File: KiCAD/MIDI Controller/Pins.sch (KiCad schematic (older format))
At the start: 25 parts, among them J10 MJ-3502, J11 MJ-3502, J12 MJ-3502, J13 MJ-3502, J14 MJ-3502, J15 MJ-3502, J16 MJ-3502, J17 MJ-3502, J5 MJ-3502, J6 MJ-3502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

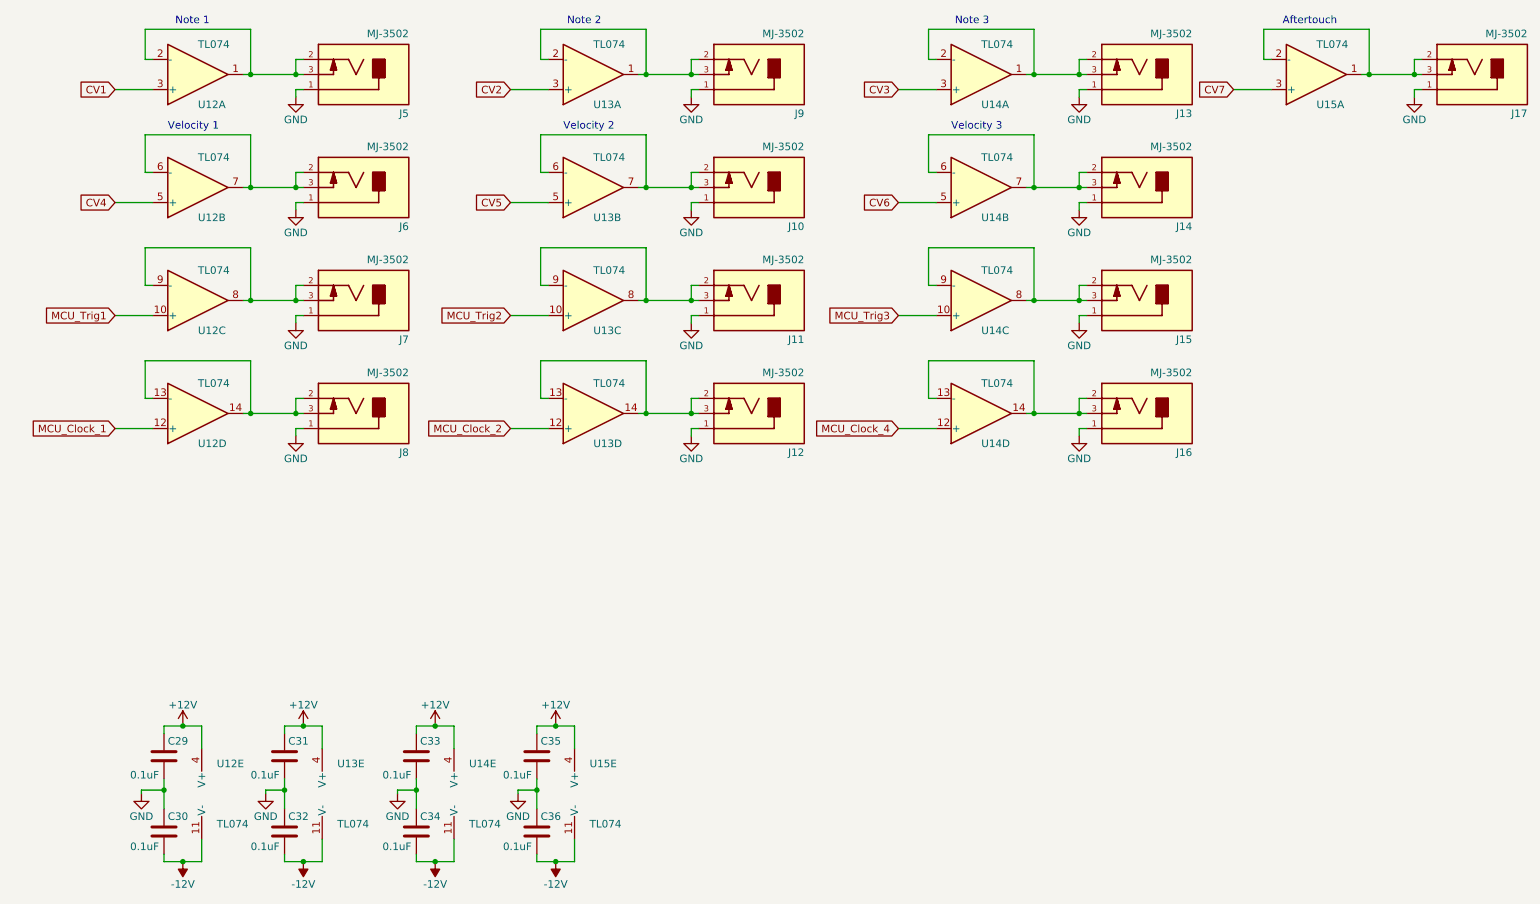
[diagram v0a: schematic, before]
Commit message: Added MIDI controller and PSU
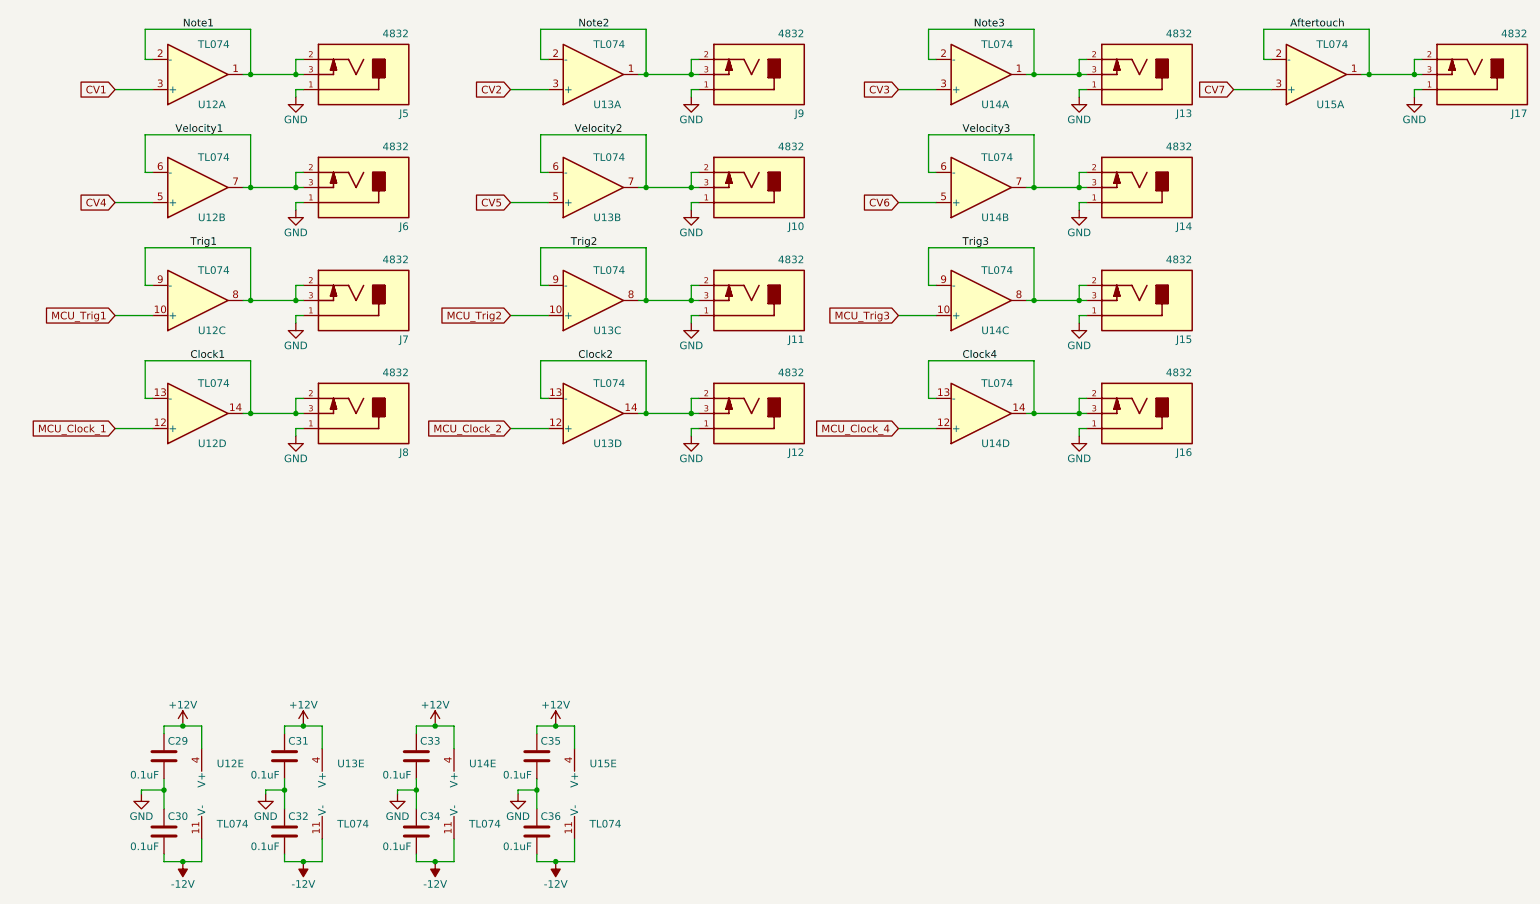
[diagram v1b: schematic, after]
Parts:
- C29, C30, C31, C32, C33, C34, C35, C36: Digikey Link (none) -> https://www.digikey.com/short/p4nr3m; Digikey PN (none) -> 720-1540-1-ND; Unit Price (none) -> 0.237
- J10, J11, J12, J13, J14, J15, J16, J17, J5, J6, J7, J8, J9: value MJ-3502 -> 4832; footprint Connector_PinHeader_2.54mm:PinHeader_1x02_P2.54mm_Vertical -> Synth:Schurter_4832_Jack; Digikey Link (none) -> https://www.digikey.com/short/p4nrqw; Digikey PN (none) -> 486-3418-ND; Field4 CP-3502MJ-ND -> (none); Field5 None -> (none); Field6 MJ-3502 -> (none); Field7 https://www.cui.com/product/interconnect/connectors/audio-c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 -> (none); Field8 3.5 mm, Mono, Right Angle, Through Hole, Threaded Bushing, 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 -> (none); Field9 CUI Inc. -> (none); Unit Price (none) -> 1.50
- U12, U13, U14, U15: Digikey Link (none) -> https://www.digikey.com/short/p4nr82; Digikey PN (none) -> 296-1283-1-ND; Unit Price (none) -> 0.60
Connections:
- net Note1: now reaches J5.2, J5.3, U12.1, U12.2 (-)
- net Velocity1: now reaches J6.2, J6.3, U12.6 (-), U12.7
- net Trig1: now reaches J7.2, J7.3, U12.8, U12.9 (-)
- net Clock1: now reaches J8.2, J8.3, U12.13 (-), U12.14
- net Note2: now reaches J9.2, J9.3, U13.1, U13.2 (-)
- net Velocity2: now reaches J10.2, J10.3, U13.6 (-), U13.7
- net Trig2: now reaches J11.2, J11.3, U13.8, U13.9 (-)
- net Clock2: now reaches J12.2, J12.3, U13.13 (-), U13.14
- net Note3: now reaches J13.2, J13.3, U14.1, U14.2 (-)
- net Velocity3: now reaches J14.2, J14.3, U14.6 (-), U14.7
- net Trig3: now reaches J15.2, J15.3, U14.8, U14.9 (-)
- net Clock4: now reaches J16.2, J16.3, U14.13 (-), U14.14
- net Aftertouch: now reaches J17.2, J17.3, U15.1, U15.2 (-)
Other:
- note removed: "Aftertouch"
- note removed: "Note 1"
- note removed: "Note 2"
- note removed: "Note 3"
- note removed: "Velocity 1"
- note removed: "Velocity 2"
- note removed: "Velocity 3"
